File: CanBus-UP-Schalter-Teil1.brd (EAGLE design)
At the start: 50 x 50 mm, 8 parts, among them K1 36.11, K2 36.11, X1 MKDSN1,5/3-5,08, X2 MKDSN1,5/3-5,08

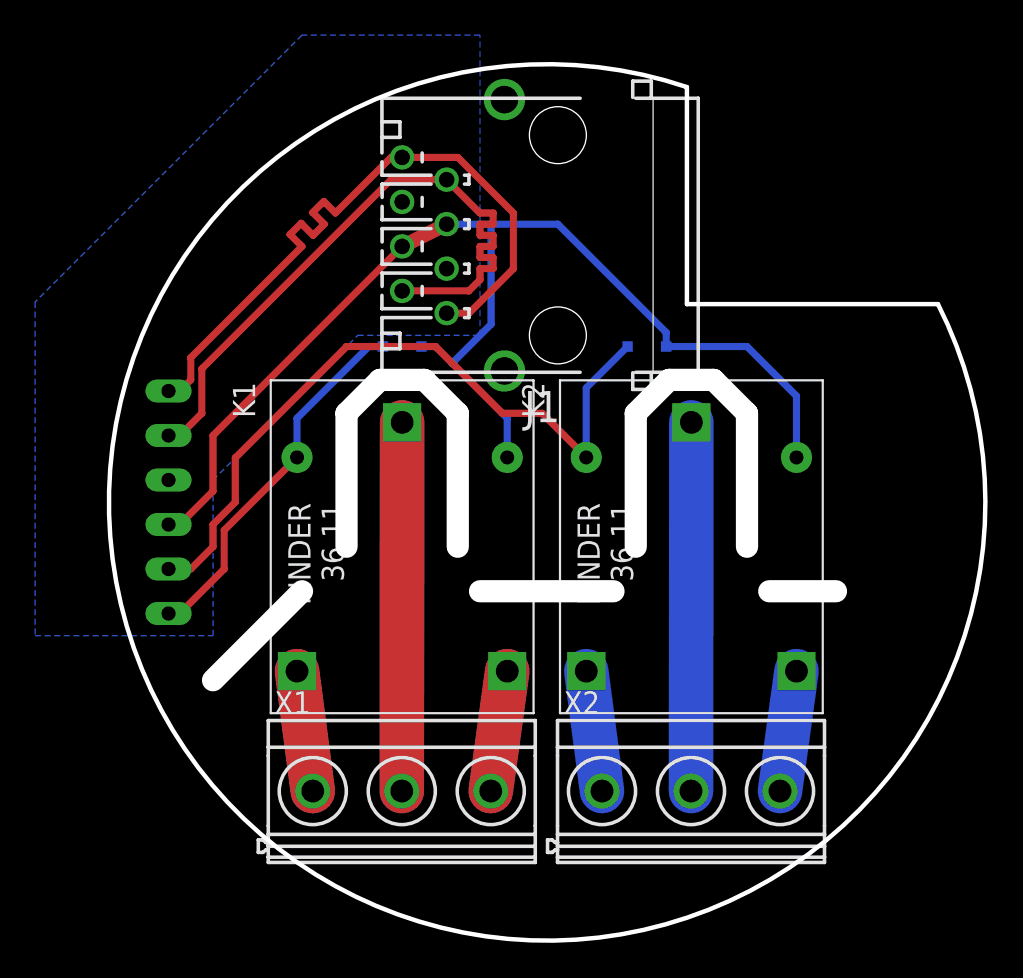
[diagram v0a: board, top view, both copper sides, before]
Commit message: Updated CAN-Bus UP-Schalter
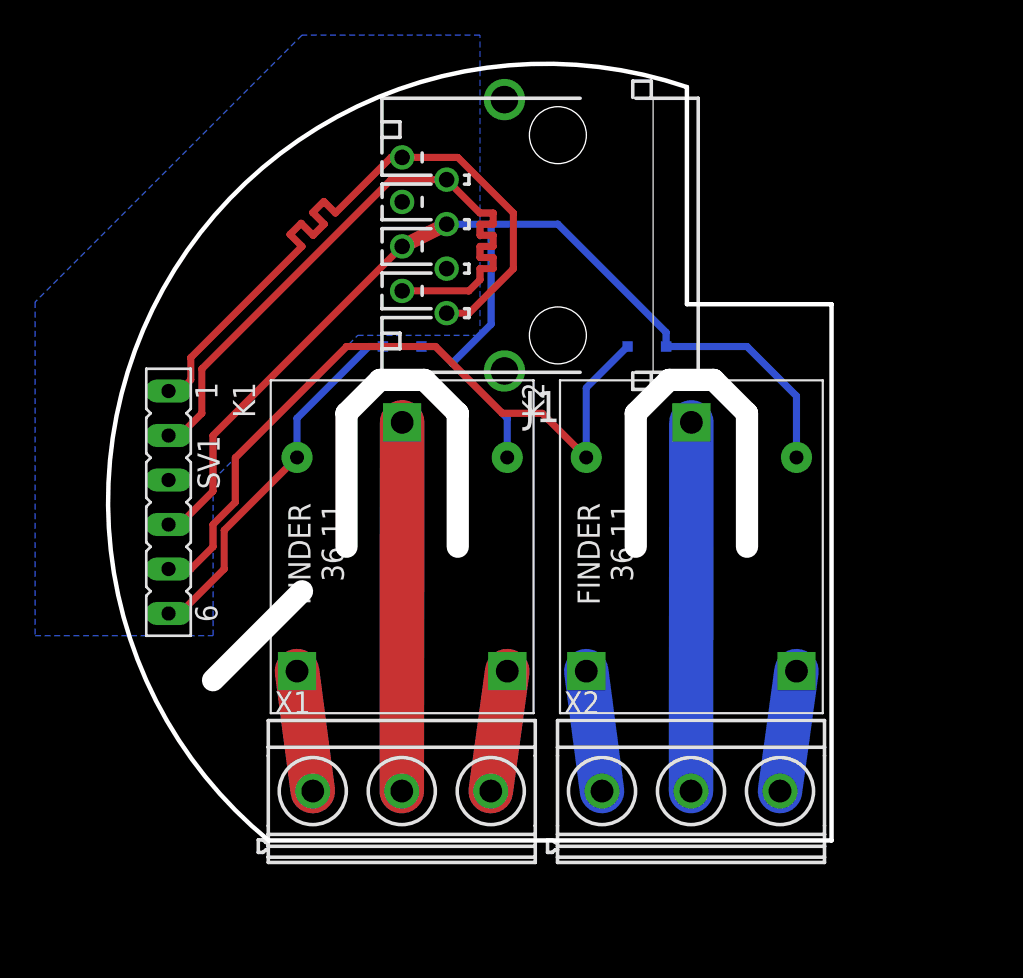
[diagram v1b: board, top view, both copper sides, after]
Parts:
- flipped SV1 to the top
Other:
- board size 50 x 50 mm -> 41.3 x 44.3 mm
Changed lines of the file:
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@@
 <setting verticaltext="up"/>
 </settings>
-<grid distance="1.27" unitdist="mm" unit="mil" style="lines" multiple="1" display="yes" altdistance="0.025" altunitdist="inch" altunit="inch"/>
+<grid distance="5" unitdist="mil" unit="mil" style="lines" multiple="1" display="yes" altdistance="0.025" altunitdist="inch" altunit="inch"/>
 <layers>
 <layer number="1" name="Top" color="4" fill="1" visible="yes" active="yes"/>
@@
 <plain>
 <wire x1="8" y1="23.7" x2="8" y2="11.31" width="0.254" layer="20"/>
-<wire x1="8" y1="11.31" x2="22.33" y2="11.31" width="0.254" layer="20"/>
-<wire x1="8" y1="23.7" x2="22.33" y2="11.31" width="0.254" layer="20" curve="315.5"/>
+<wire x1="8" y1="23.7" x2="-15.875" y2="-19.304" width="0.254" layer="20" curve="159.5"/>
 <wire x1="-6.985" y1="6.985" x2="-5.08" y2="5.08" width="1.27" layer="46"/>
 <wire x1="-5.08" y1="5.08" x2="-5.08" y2="-2.54" width="1.27" layer="46"/>
@@
 <wire x1="5.08" y1="5.08" x2="5.08" y2="-2.54" width="1.27" layer="46"/>
 <wire x1="-13.97" y1="-5.08" x2="-19.05" y2="-10.16" width="1.27" layer="46"/>
-<wire x1="-3.81" y1="-5.08" x2="3.81" y2="-5.08" width="1.27" layer="46"/>
-<wire x1="12.7" y1="-5.08" x2="16.51" y2="-5.08" width="1.27" layer="46"/>
+<wire x1="16.256" y1="11.303" x2="16.256" y2="-19.304" width="0.254" layer="20"/>
+<wire x1="16.256" y1="-19.304" x2="-15.875" y2="-19.304" width="0.254" layer="20"/>
+<circle x="0" y="0" radius="25" width="0.1" layer="48"/>
+<wire x1="8.001" y1="11.303" x2="16.256" y2="11.303" width="0.254" layer="20"/>
 </plain>
 <attributes>
@@
 <element name="D1" library="diode" package="SOD323-R" value="" x="-8.255" y="8.89" rot="MR0"/>
 <element name="D2" library="diode" package="SOD323-R" value="" x="5.715" y="8.89" rot="MR0"/>
-<element name="SV1" library="con-lsta" package="FE06" value="" x="-21.59" y="0" rot="MR270">
-<attribute name="MF" value="" x="-21.59" y="0" size="1.778" layer="28" rot="MR270" display="off"/>
-<attribute name="MPN" value="" x="-21.59" y="0" size="1.778" layer="28" rot="MR270" display="off"/>
-<attribute name="OC_FARNELL" value="unknown" x="-21.59" y="0" size="1.778" layer="28" rot="MR270" display="off"/>
-<attribute name="OC_NEWARK" value="unknown" x="-21.59" y="0" size="1.778" layer="28" rot="MR270" display="off"/>
+<element name="SV1" library="con-lsta" package="FE06" value="" x="-21.59" y="0" rot="R270">
+<attribute name="MF" value="" x="-21.59" y="0" size="1.778" layer="27" rot="R270" display="off"/>
+<attribute name="MPN" value="" x="-21.59" y="0" size="1.778" layer="27" rot="R270" display="off"/>
+<attribute name="OC_FARNELL" value="unknown" x="-21.59" y="0" size="1.778" layer="27" rot="R270" display="off"/>
+<attribute name="OC_NEWARK" value="unknown" x="-21.59" y="0" size="1.778" layer="27" rot="R270" display="off"/>
 </element>
 </elements>

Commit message: CAN-Schield hinzugefügt, CanBus-UP-Schalter fertiggestellt
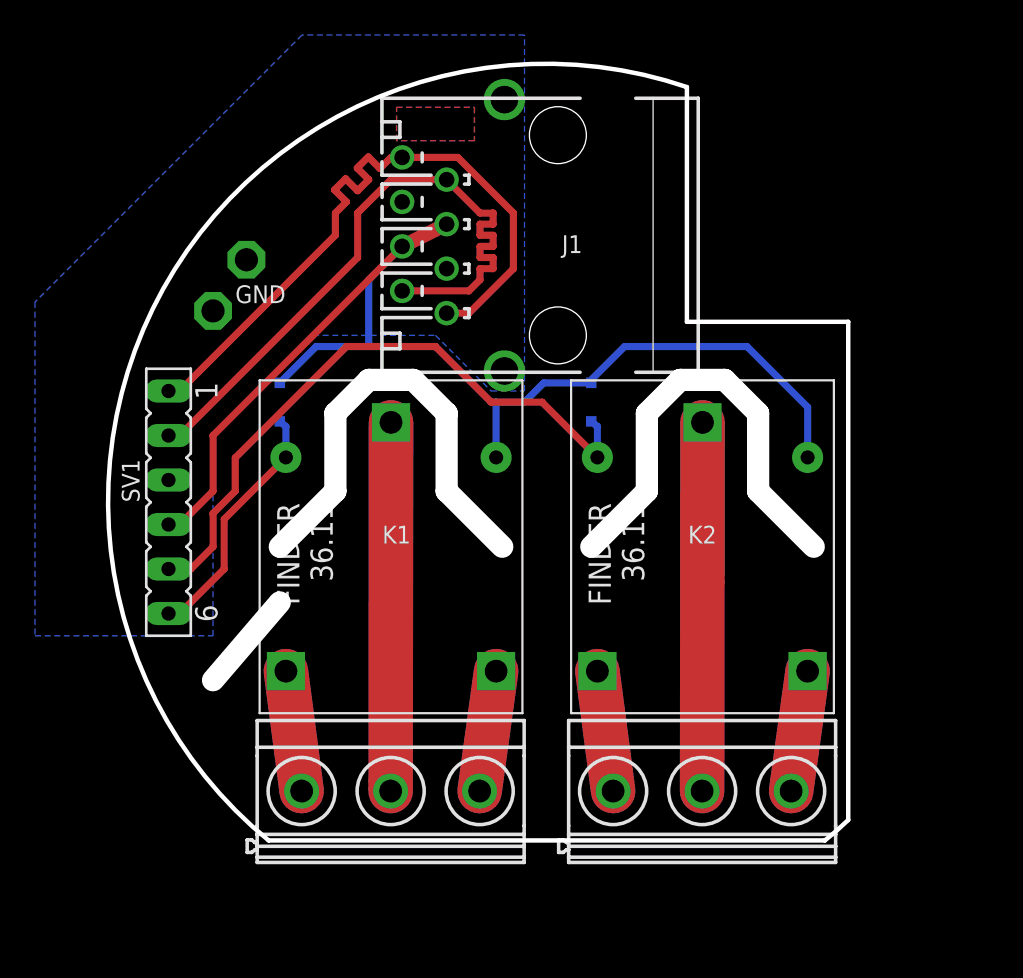
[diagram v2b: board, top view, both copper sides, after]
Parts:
- added LSP1, LSP2: LSP13, solpad:LSP13
- J1: device mebp_8-8g:MEBP_8-8G -> can-bus:MEBP_8-8G
- moved D1 7.67 mm to (-15.2, 5.71), turned to 270 degrees
- moved D2 4.49 mm to (2.54, 5.71), turned to 270 degrees
- moved K1 0.63 mm to (-8.89, -2.54)
- moved K2 0.63 mm to (8.89, -2.54)
- moved X1 0.63 mm to (-6.35, -16.5)
- moved X2 0.63 mm to (11.4, -16.5)
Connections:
- net GND: now also J1.G1, J1.G2, LSP1.MP, LSP2.MP
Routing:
- net N$6: track 21.0 -> 42.1 mm
- net N$4: track 6.91 -> 13.8 mm
- net N$5: track 6.90 -> 13.8 mm
- net RELAIS_1: track 21.2 -> 14.3 mm
- net RELAIS_2: track 41.3 -> 36.8 mm
- net +24V: track 70.3 -> 72.3 mm
- added copper zone on layer 16, net BOT
- added copper zone on layer 1, net TOP
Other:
- board size 41.3 x 44.3 mm -> 42.2 x 44.3 mm
- board text added: "BOT"
- board text added: "GND"
- board text added: "NC"
- board text added: "NO"
- board text added: "TOP"

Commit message: CanBus-UP-Schalter fertiggestellt
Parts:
- removed J1: (no value), can-bus:MEBP_8-8G
- added LSP3, LSP4, LSP5, LSP6: LSP13, solpad:LSP13
- added SV2: (no value), can-bus:ML10L
- moved LSP1 4.45 mm to (-12.7, 14.0)
- moved LSP2 3.97 mm to (-16.5, 14.0)
- moved D1 0.32 mm to (-14.9, 5.71)
- moved D2 0.32 mm to (2.86, 5.71)
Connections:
- net +24V: now also LSP6.MP, SV2.4, SV2.5; no longer J1.4, J1.5
- net CANH: now also SV2.2, SV2.7; no longer J1.2, J1.7
- net CANL: now also SV2.1, SV2.8; no longer J1.1, J1.8
- net GND: now also LSP3.MP, LSP4.MP, LSP5.MP, SV2.3, SV2.6; no longer J1.3, J1.6, J1.G1, J1.G2
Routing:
- net +24V: track 72.3 -> 59.8 mm, vias 0 -> 1
- net CANL: track 39.1 -> 32.8 mm
- net CANH: track 39.1 -> 33.8 mm, vias 0 -> 2
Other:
- board size 42.2 x 44.3 mm -> 42.2 x 40.1 mm
- board text added: "!! 230 V !!"
- board text added: "+24V"
- board text added: "L"
